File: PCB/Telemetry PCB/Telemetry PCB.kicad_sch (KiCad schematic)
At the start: 36 parts, among them IC1 E22-900M22S, J1 Conn_01x04_Pin, J2 GPS, J3 Batt, SW1 SW_MEC_5E, SW2 SW_MEC_5E, U1 STM32F411CEUx, U2 AP62200WU, Y1 25MHZ 9pF, Y2 32.768k 6pF

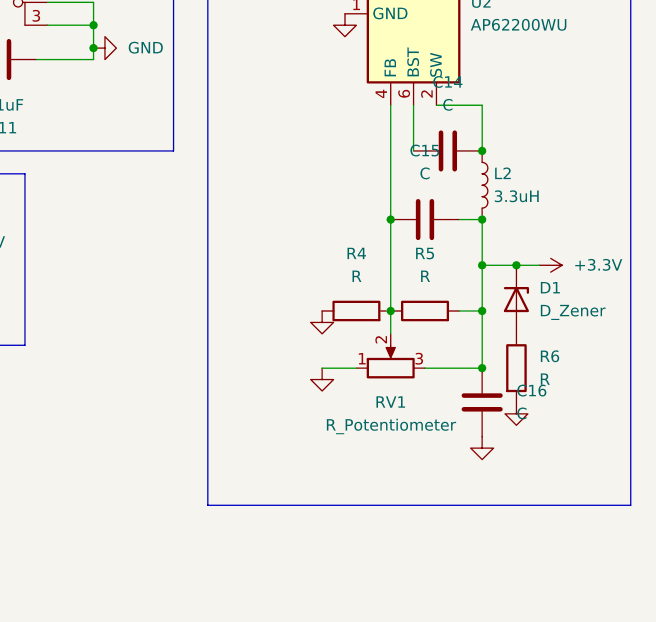
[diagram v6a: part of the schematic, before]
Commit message: removed potentiometer and replaced with exact value resistors
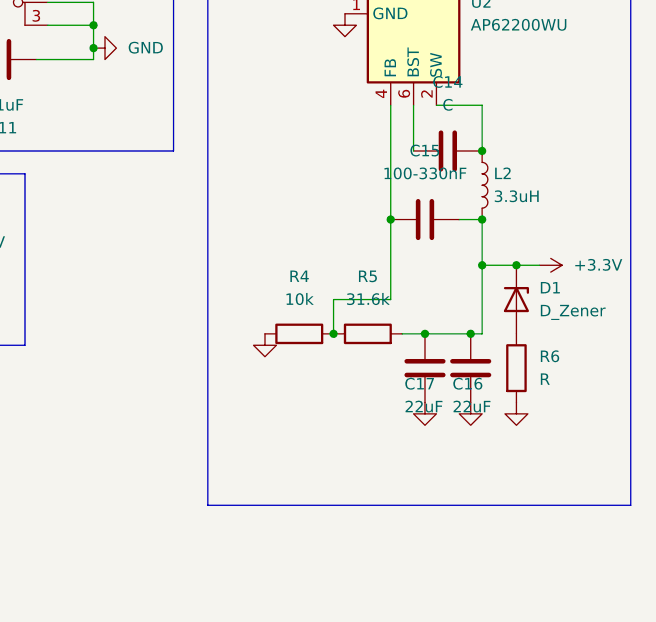
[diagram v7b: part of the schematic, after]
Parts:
- removed RV1: R_Potentiometer, symbol Device:R_Potentiometer
- added C17: 22uF, symbol Device:C
- C15: value C -> 100-330nF
- C16: value C -> 22uF
- R4: value R -> 10k
- R5: value R -> 31.6k
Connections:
- net +3.3V: now also C17.2
- net GND: now also C17.1
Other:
- moved on the sheet: C16, R4, R5
